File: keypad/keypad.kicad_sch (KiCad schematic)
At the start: 0 parts

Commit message: Scheme 1.0 complete
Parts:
- added C1, C2, C3, C4: 0.1u, symbol Device:C_Small
- added C5: 10u, symbol Device:C_Small
- added C? (x2): 22p, symbol Device:C_Small
- added C?: 1u, symbol Device:C_Small
- added F?: 500mA, symbol Device:Polyfuse_Small
- added J?: AVR-ISP-6, symbol Connector:AVR-ISP-6
- added R? (x2): 5.1k, symbol Device:R_Small
- added R? (x2): 22, symbol Device:R_Small
- added R? (x2): 10k, symbol Device:R_Small
- added SW?: SW_Push_Reset, symbol SW_SKQG:SW_SKQG
- added U?: PRTR5V0U2X, symbol random-keyboard-parts:PRTR5V0U2X
- added U?: ATMEGA32U4-AU, QFP80P1200X1200X120-44N, symbol ATMEGA32U4-AU:ATMEGA32U4-AU
- added USB?: HRO-TYPE-C-31-M-12, symbol Type-C:HRO-TYPE-C-31-M-12
- added Y?: XTAL, symbol Device:Crystal_GND24_Small
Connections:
- new net: R?.2, USB?.4 (CC1)
- new net: R?.2, USB?.10 (CC2)
- new net: R?.1, U?.3 (IO2), USB?.5 (DN2), USB?.7 (DN1)
- new net: R?.1, U?.2 (IO1), USB?.6 (DP1), USB?.8 (DP2)
- new net: R?.1, U?.33 (PE2)
- new net: C?.1, U?.6 (UCAP)
- new net +5V: C1.1, C2.1, C3.1, C4.1, C5.1, F?.2, J?.2 (VCC), R?.1, U?.14 (VCC), U?.2 (UVCC), U?.24 (AVCC), U?.34 (VCC), U?.44 (AVCC), U?.7 (VBUS)
- new net D+: R?.2, U?.4 (D+)
- new net D-: R?.2, U?.3 (D-)
- new net GND: C1.2, C2.2, C3.2, C4.2, C5.2, C?.2, C?.2, C?.2, J?.6 (GND), R?.1, R?.1, R?.2, SW?.2 (ve), U?.1 (GND), U?.15 (GND), U?.23 (GND), U?.35 (GND), U?.43 (GND), U?.5 (UGND), USB?.1 (GND), USB?.12 (GND), USB?.13 (SHIELD), Y?.2, Y?.4
- new net MISO: J?.1 (MISO), U?.11 (PB3)
- new net MOSI: J?.4 (MOSI), U?.10 (PB2)
- new net Reset: J?.5 (~{RST}), R?.2, SW?.1 (ve), U?.13 (~{RESET})
- new net SCK: J?.3 (SCK), U?.9 (PB1)
- new net VCC: F?.1, U?.4 (VCC), USB?.11 (VBUS), USB?.2 (VBUS)
- new net XTAL1: C?.1, U?.17 (XTAL1), Y?.1
- new net XTAL2: C?.1, U?.16 (XTAL2), Y?.3
- no-connect marks 0 -> 5

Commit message: Creat Matrix 1.0
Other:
- added sheet matrix (matrix.kicad_sch)
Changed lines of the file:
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@@
     (pin "2")
+  )
+  (sheet (at 260.35 158.75) (size 12.7 3.81) (fields_autoplaced)
+    (stroke (width 0.1524) (type solid) (color 0 0 0 0))
+    (fill (color 0 0 0 0.0000))
+    (property "Sheet name" "matrix" (id 0) (at 260.35 158.0384 0)
+      (effects (font (size 1.27 1.27)) (justify left bottom))
+    )
+    (property "Sheet file" "matrix.kicad_sch" (id 1) (at 260.35 163.1446 0)
+      (effects (font (size 1.27 1.27)) (justify left top))
+    )
   )
   (sheet_instances
     (path "/" (page "1"))
+    (path "/5536efe7-c8bb-4c6c-93af-3db80ade0fb5" (page "2"))
   )
   (symbol_instances
@@
       (reference "C?") (unit 1) (value "22p") (footprint "")
     )
+    (path "/5536efe7-c8bb-4c6c-93af-3db80ade0fb5/9a644794-52ea-4327-bd09-f8b15524fedf"
+      (reference "D1") (unit 1) (value "D") (footprint "")
+    )
+    (path "/5536efe7-c8bb-4c6c-93af-3db80ade0fb5/b4841a33-c386-479d-996e-ba2927116e58"
+      (reference "D2") (unit 1) (value "D") (footprint "")
+    )
+    (path "/5536efe7-c8bb-4c6c-93af-3db80ade0fb5/79e7db55-38f0-4a73-ab95-a7bab10db2bc"
+      (reference "D3") (unit 1) (value "D") (footprint "")
+    )
+    (path "/5536efe7-c8bb-4c6c-93af-3db80ade0fb5/f561a5ac-3059-4521-99af-42498ff48bbe"
+      (reference "D4") (unit 1) (value "D") (footprint "")
+    )
+    (path "/5536efe7-c8bb-4c6c-93af-3db80ade0fb5/c448c4ba-7a95-4e8b-868a-fbc34300787c"
+      (reference "D5") (unit 1) (value "D") (footprint "")
+    )
+    (path "/5536efe7-c8bb-4c6c-93af-3db80ade0fb5/e07c9ef6-5451-425c-9e0a-962144539f5d"
+      (reference "D6") (unit 1) (value "D") (footprint "")
+    )
+    (path "/5536efe7-c8bb-4c6c-93af-3db80ade0fb5/78d23edb-643f-406e-b146-b9943f76ab45"
+      (reference "D7") (unit 1) (value "D") (footprint "")
+    )
+    (path "/5536efe7-c8bb-4c6c-93af-3db80ade0fb5/89fcd485-e50f-416d-9f08-898bba03eec0"
+      (reference "D8") (unit 1) (value "D") (footprint "")
+    )
+    (path "/5536efe7-c8bb-4c6c-93af-3db80ade0fb5/7c6547ba-1358-4c6c-8003-39bdd1f7d938"
+      (reference "D9") (unit 1) (value "D") (footprint "")
+    )
+    (path "/5536efe7-c8bb-4c6c-93af-3db80ade0fb5/67ecc62a-8f0d-4b3a-b4c1-b1c6e1ca890f"
+      (reference "D10") (unit 1) (value "D") (footprint "")
+    )
+    (path "/5536efe7-c8bb-4c6c-93af-3db80ade0fb5/bc75af07-bd2c-4b47-b0fb-1f1929983761"
+      (reference "D11") (unit 1) (value "D") (footprint "")
+    )
+    (path "/5536efe7-c8bb-4c6c-93af-3db80ade0fb5/280455c7-3c8b-418f-a011-da03396841a7"
+      (reference "D12") (unit 1) (value "D") (footprint "")
+    )
+    (path "/5536efe7-c8bb-4c6c-93af-3db80ade0fb5/c2839c0b-9c65-4167-8039-ba7e2d9fec9d"
+      (reference "D13") (unit 1) (value "D") (footprint "")
+    )
+    (path "/5536efe7-c8bb-4c6c-93af-3db80ade0fb5/de303921-c38f-4c10-aba0-b46505fdefbf"
+      (reference "D14") (unit 1) (value "D") (footprint "")
+    )
+    (path "/5536efe7-c8bb-4c6c-93af-3db80ade0fb5/bdbe8408-effe-4323-8624-7153e57df912"
+      (reference "D15") (unit 1) (value "D") (footprint "")
+    )
+    (path "/5536efe7-c8bb-4c6c-93af-3db80ade0fb5/687984bd-da5f-4098-8907-2694332a2741"
+      (reference "D16") (unit 1) (value "D") (footprint "")
+    )
+    (path "/5536efe7-c8bb-4c6c-93af-3db80ade0fb5/72dba145-79d1-42aa-a952-0fcd5dbb5f51"
+      (reference "D17") (unit 1) (value "D") (footprint "")
+    )
+    (path "/5536efe7-c8bb-4c6c-93af-3db80ade0fb5/359023dd-c07d-4d1f-8a68-2798543f6791"
+      (reference "D18") (unit 1) (value "D") (footprint "")
+    )
+    (path "/5536efe7-c8bb-4c6c-93af-3db80ade0fb5/ec1a4f44-ed28-469d-bce4-39f6b11d96b0"
+      (reference "D19") (unit 1) (value "D") (footprint "")
+    )
     (path "/8191da82-1b24-43f7-89f2-5c294481326b"
       (reference "F?") (unit 1) (value "500mA") (footprint "")
@@
       (reference "R?") (unit 1) (value "22") (footprint "")
     )
+    (path "/5536efe7-c8bb-4c6c-93af-3db80ade0fb5/a8fbe275-e45a-4f46-aab6-af2a9be66cc7"
+      (reference "SW1") (unit 1) (value "num") (footprint "")
+    )
+    (path "/5536efe7-c8bb-4c6c-93af-3db80ade0fb5/90daedf7-5a7f-4c03-b61a-54b82546f0ae"
+      (reference "SW2") (unit 1) (value "div") (footprint "")
+    )
+    (path "/5536efe7-c8bb-4c6c-93af-3db80ade0fb5/6320b691-9818-4d75-b444-8163a922571d"
+      (reference "SW3") (unit 1) (value "mult") (footprint "")
+    )
+    (path "/5536efe7-c8bb-4c6c-93af-3db80ade0fb5/52d3a178-efab-47c5-a04f-7b9702ec7191"
+      (reference "SW4") (unit 1) (value "min") (footprint "")
+    )
+    (path "/5536efe7-c8bb-4c6c-93af-3db80ade0fb5/900f3076-96ff-42d7-a6f8-6e5918b538b7"
+      (reference "SW5") (unit 1) (value "#7") (footprint "")
+    )
+    (path "/5536efe7-c8bb-4c6c-93af-3db80ade0fb5/3423f380-322d-4e75-85ef-f42ce1034340"
+      (reference "SW6") (unit 1) (value "#8") (footprint "")
+    )
+    (path "/5536efe7-c8bb-4c6c-93af-3db80ade0fb5/b9ef477f-6510-4722-bbd5-47ed3b264249"
+      (reference "SW7") (unit 1) (value "#9") (footprint "")
+    )
+    (path "/5536efe7-c8bb-4c6c-93af-3db80ade0fb5/af993652-e2ec-4985-b2d6-324ab2415001"
+      (reference "SW8") (unit 1) (value "plu0") (footprint "")
+    )
+    (path "/5536efe7-c8bb-4c6c-93af-3db80ade0fb5/5a9c176c-6c6a-40aa-a0cf-ecfca809a92a"
+      (reference "SW9") (unit 1) (value "#4") (footprint "")
+    )
+    (path "/5536efe7-c8bb-4c6c-93af-3db80ade0fb5/49aa3199-5925-426d-9bbe-c5416226cedc"
+      (reference "SW10") (unit 1) (value "#5") (footprint "")
+    )
+    (path "/5536efe7-c8bb-4c6c-93af-3db80ade0fb5/edbfbc9f-fae0-4b09-8fd1-2fdb5910af52"
+      (reference "SW11") (unit 1) (value "#6") (footprint "")
+    )
+    (path "/5536efe7-c8bb-4c6c-93af-3db80ade0fb5/dd21500d-5cc3-406f-b6e4-1ac6ec593097"
+      (reference "SW12") (unit 1) (value "plu1") (footprint "")
+    )
+    (path "/5536efe7-c8bb-4c6c-93af-3db80ade0fb5/ba03b49d-f73d-4109-b19f-516cb2f4d6fa"
+      (reference "SW13") (unit 1) (value "#1") (footprint "")
+    )
+    (path "/5536efe7-c8bb-4c6c-93af-3db80ade0fb5/f13ec7a5-97d7-4169-806d-f29da36b319b"
+      (reference "SW14") (unit 1) (value "#2") (footprint "")
+    )
+    (path "/5536efe7-c8bb-4c6c-93af-3db80ade0fb5/e85cc504-ce98-4080-8b0a-822b1039c0be"
+      (reference "SW15") (unit 1) (value "#3") (footprint "")
+    )
+    (path "/5536efe7-c8bb-4c6c-93af-3db80ade0fb5/2dd3eeeb-1dda-4560-a555-7533fb4ee835"
+      (reference "SW16") (unit 1) (value "ent0") (footprint "")
+    )
+    (path "/5536efe7-c8bb-4c6c-93af-3db80ade0fb5/eb663575-2bb7-46c4-8857-4495de8fb975"
+      (reference "SW17") (unit 1) (value "#0") (footprint "")
+    )
+    (path "/5536efe7-c8bb-4c6c-93af-3db80ade0fb5/34938f56-f0c5-42e4-858d-1eefaa7132ef"
+      (reference "SW18") (unit 1) (value "kom") (footprint "")
+    )
+    (path "/5536efe7-c8bb-4c6c-93af-3db80ade0fb5/d07f8cae-5702-4915-8b31-407c3d188184"
+      (reference "SW19") (unit 1) (value "ent1") (footprint "")
+    )
     (path "/df8a378d-e0e9-4784-8be5-a23e7f34a8f8"

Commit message: Assign Footprints
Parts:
- C1, C2, C8: renamed from C?; footprint (none) -> Capacitor_SMD:C_0805_2012Metric_Pad1.18x1.45mm_HandSolder
- C3: renamed from C1; footprint (none) -> Capacitor_SMD:C_0805_2012Metric_Pad1.18x1.45mm_HandSolder
- C4: renamed from C2; footprint (none) -> Capacitor_SMD:C_0805_2012Metric_Pad1.18x1.45mm_HandSolder
- C5: renamed from C3; footprint (none) -> Capacitor_SMD:C_0805_2012Metric_Pad1.18x1.45mm_HandSolder
- C6: renamed from C4; footprint (none) -> Capacitor_SMD:C_0805_2012Metric_Pad1.18x1.45mm_HandSolder
- C7: renamed from C5; footprint (none) -> Capacitor_SMD:C_0805_2012Metric_Pad1.18x1.45mm_HandSolder
- F1: renamed from F?; footprint (none) -> Fuse:Fuse_1206_3216Metric_Pad1.42x1.75mm_HandSolder
- J1: renamed from J?; footprint (none) -> random-keyboard-parts:Reset_Pretty-Mask
- R1, R2, R3, R4, R5, R6: renamed from R?; footprint (none) -> Resistor_SMD:R_0805_2012Metric_Pad1.20x1.40mm_HandSolder
- SW20: renamed from SW?; footprint (none) -> Button_Switch_SMD:SW_SPST_SKQG_WithStem
- U1: renamed from U?; footprint (none) -> random-keyboard-parts:SOT143B
- U2: renamed from U?; footprint QFP80P1200X1200X120-44N -> ATMEGA32U4-AU:QFP80P1200X1200X120-44N
- USB1: renamed from USB?; footprint (none) -> Type-C:HRO-TYPE-C-31-M-12-HandSoldering
- Y1: renamed from Y?; footprint (none) -> Crystal:Crystal_SMD_3225-4Pin_3.2x2.5mm_HandSoldering
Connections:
- net col2: now reaches U2.29 (PB5)
- net col3: now reaches U2.30 (PB6)
- net col1: now reaches U2.31 (PC6)
- net col0: now reaches U2.32 (PC7)
- net row4: now reaches U2.37 (PF6)
- net row3: now reaches U2.38 (PF5)
- net row2: now reaches U2.39 (PF4)
- net row1: now reaches U2.40 (PF1)
- net row0: now reaches U2.41 (PF0)
- no-connect marks 5 -> 18

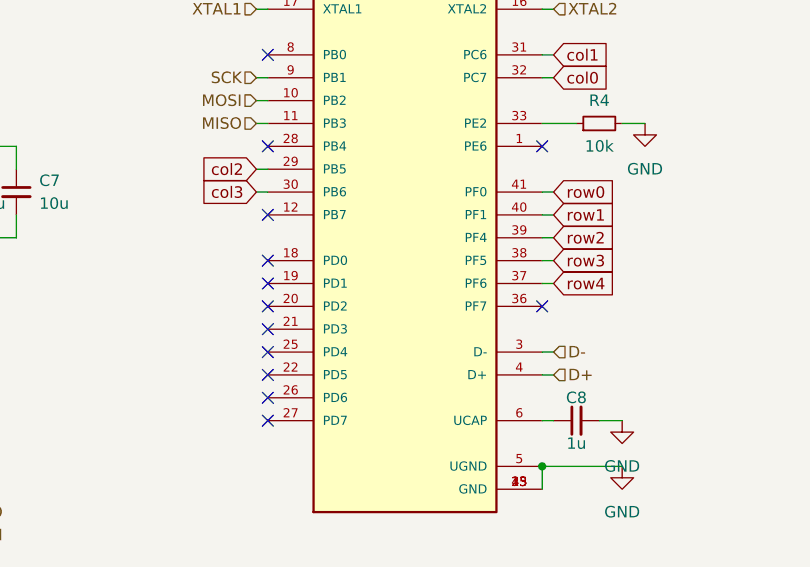
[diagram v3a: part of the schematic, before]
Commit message: Fixed Layering
Also as a note, there was a rogue 1uF capacitor which I now just placed under the usb, out of the way. It may be needed later.
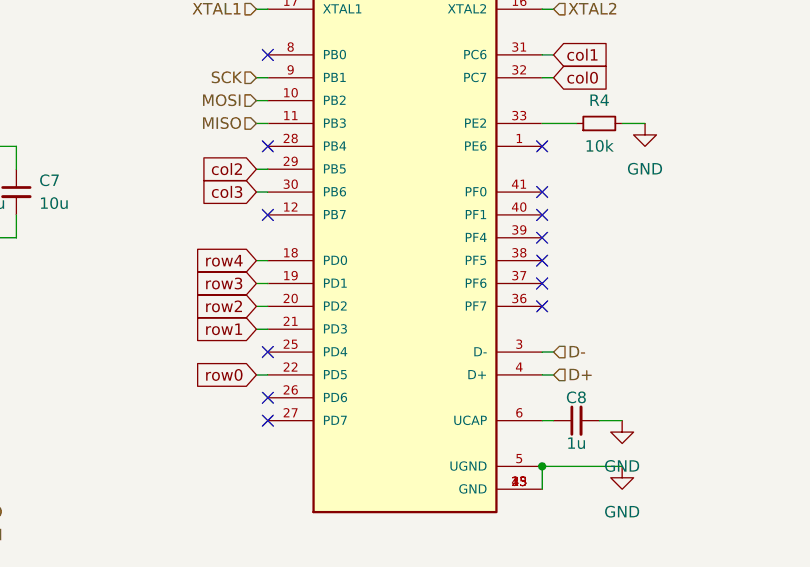
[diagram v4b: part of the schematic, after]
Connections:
- net row0: now also U2.22 (PD5); no longer U2.41 (PF0)
- net row1: now also U2.21 (PD3); no longer U2.40 (PF1)
- net row2: now also U2.20 (PD2); no longer U2.39 (PF4)
- net row3: now also U2.19 (PD1); no longer U2.38 (PF5)
- net row4: now also U2.18 (PD0); no longer U2.37 (PF6)
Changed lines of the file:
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@@
   (no_connect (at 63.5 68.58))
   (no_connect (at 129.54 109.22))
-  (no_connect (at 99.06 109.22))
+  (no_connect (at 129.54 101.6))
   (no_connect (at 207.01 68.58))
-  (no_connect (at 99.06 111.76))
   (no_connect (at 99.06 81.28))
+  (no_connect (at 129.54 99.06))
   (no_connect (at 99.06 91.44))
   (no_connect (at 99.06 68.58))
   (no_connect (at 50.8 63.5))
   (no_connect (at 99.06 119.38))
-  (no_connect (at 99.06 104.14))
-  (no_connect (at 99.06 116.84))
   (no_connect (at 129.54 91.44))
   (no_connect (at 207.01 83.82))
   (no_connect (at 99.06 121.92))
+  (no_connect (at 129.54 104.14))
   (no_connect (at 99.06 99.06))
+  (no_connect (at 129.54 96.52))
   (no_connect (at 99.06 114.3))
-  (no_connect (at 99.06 106.68))
+  (no_connect (at 129.54 106.68))
   (wire (pts (xy 71.12 93.98) (xy 71.12 91.44))
     (stroke (width 0) (type default) (color 0 0 0 0))
@@
     (stroke (width 0) (type default) (color 0 0 0 0))
   )
+  (wire (pts (xy 97.79 104.14) (xy 99.06 104.14))
+    (stroke (width 0) (type default) (color 0 0 0 0))
+  )
   (wire (pts (xy 63.5 63.5) (xy 64.77 63.5))
     (stroke (width 0) (type default) (color 0 0 0 0))
@@
     (stroke (width 0) (type default) (color 0 0 0 0))
   )
-  (wire (pts (xy 129.54 96.52) (xy 130.81 96.52))
-    (stroke (width 0) (type default) (color 0 0 0 0))
-  )
   (wire (pts (xy 207.01 86.36) (xy 214.63 86.36))
     (stroke (width 0) (type default) (color 0 0 0 0))
@@
     (stroke (width 0) (type default) (color 0 0 0 0))
   )
+  (wire (pts (xy 97.79 116.84) (xy 99.06 116.84))
+    (stroke (width 0) (type default) (color 0 0 0 0))
+  )
   (wire (pts (xy 208.28 63.5) (xy 208.28 91.44))
     (stroke (width 0) (type default) (color 0 0 0 0))
@@
     (stroke (width 0) (type default) (color 0 0 0 0))
   )
-  (wire (pts (xy 129.54 99.06) (xy 130.81 99.06))
-    (stroke (width 0) (type default) (color 0 0 0 0))
-  )
   (wire (pts (xy 85.09 45.72) (xy 85.09 46.99))
     (stroke (width 0) (type default) (color 0 0 0 0))
@@
     (stroke (width 0) (type default) (color 0 0 0 0))
   )
+  (wire (pts (xy 97.79 111.76) (xy 99.06 111.76))
+    (stroke (width 0) (type default) (color 0 0 0 0))
+  )
   (wire (pts (xy 71.12 101.6) (xy 63.5 101.6))
     (stroke (width 0) (type default) (color 0 0 0 0))
@@
     (stroke (width 0) (type default) (color 0 0 0 0))
   )
-  (wire (pts (xy 129.54 104.14) (xy 130.81 104.14))
+  (wire (pts (xy 97.79 109.22) (xy 99.06 109.22))
     (stroke (width 0) (type default) (color 0 0 0 0))
   )
@@
     (stroke (width 0) (type default) (color 0 0 0 0))
   )
+  (wire (pts (xy 97.79 106.68) (xy 99.06 106.68))
+    (stroke (width 0) (type default) (color 0 0 0 0))
+  )
   (wire (pts (xy 87.63 43.18) (xy 91.44 43.18))
     (stroke (width 0) (type default) (color 0 0 0 0))
@@
     (stroke (width 0) (type default) (color 0 0 0 0))
   )
-  (wire (pts (xy 129.54 101.6) (xy 130.81 101.6))
-    (stroke (width 0) (type default) (color 0 0 0 0))
-  )
   (wire (pts (xy 208.28 93.98) (xy 212.09 93.98))
     (stroke (width 0) (type default) (color 0 0 0 0))
   )
-  (wire (pts (xy 129.54 106.68) (xy 130.81 106.68))
-    (stroke (width 0) (type default) (color 0 0 0 0))
-  )
   (wire (pts (xy 213.36 76.2) (xy 213.36 81.28))
     (stroke (width 0) (type default) (color 0 0 0 0))
@@
     (stroke (width 0) (type default) (color 0 0 0 0))
   )
-  (global_label "row4" (shape input) (at 130.81 106.68 0) (fields_autoplaced)
-    (effects (font (size 1.27 1.27)) (justify left))
-    (property "Intersheet References" "${INTERSHEET_REFS}" (id 0) (at 137.6983 106.6006 0)
-      (effects (font (size 1.27 1.27)) (justify left) hide)
+  (global_label "row4" (shape input) (at 97.79 104.14 180) (fields_autoplaced)
+    (effects (font (size 1.27 1.27)) (justify right))
+    (property "Intersheet References" "${INTERSHEET_REFS}" (id 0) (at 90.9017 104.2194 0)
+      (effects (font (size 1.27 1.27)) (justify right) hide)
     )
   )
@@
     )
   )
-  (global_label "row1" (shape input) (at 130.81 99.06 0) (fields_autoplaced)
-    (effects (font (size 1.27 1.27)) (justify left))
-    (property "Intersheet References" "${INTERSHEET_REFS}" (id 0) (at 137.6983 98.9806 0)
-      (effects (font (size 1.27 1.27)) (justify left) hide)
-    )
-  )
-  (global_label "row0" (shape input) (at 130.81 96.52 0) (fields_autoplaced)
-    (effects (font (size 1.27 1.27)) (justify left))
-    (property "Intersheet References" "${INTERSHEET_REFS}" (id 0) (at 137.6983 96.4406 0)
-      (effects (font (size 1.27 1.27)) (justify left) hide)
-    )
-  )
-  (global_label "row2" (shape input) (at 130.81 101.6 0) (fields_autoplaced)
-    (effects (font (size 1.27 1.27)) (justify left))
-    (property "Intersheet References" "${INTERSHEET_REFS}" (id 0) (at 137.6983 101.5206 0)
-      (effects (font (size 1.27 1.27)) (justify left) hide)
+  (global_label "row1" (shape input) (at 97.79 111.76 180) (fields_autoplaced)
+    (effects (font (size 1.27 1.27)) (justify right))
+    (property "Intersheet References" "${INTERSHEET_REFS}" (id 0) (at 90.9017 111.8394 0)
+      (effects (font (size 1.27 1.27)) (justify right) hide)
+    )
+  )
+  (global_label "row0" (shape input) (at 97.79 116.84 180) (fields_autoplaced)
+    (effects (font (size 1.27 1.27)) (justify right))
+    (property "Intersheet References" "${INTERSHEET_REFS}" (id 0) (at 90.9017 116.9194 0)
+      (effects (font (size 1.27 1.27)) (justify right) hide)
+    )
+  )
+  (global_label "row2" (shape input) (at 97.79 109.22 180) (fields_autoplaced)
+    (effects (font (size 1.27 1.27)) (justify right))
+    (property "Intersheet References" "${INTERSHEET_REFS}" (id 0) (at 90.9017 109.2994 0)
+      (effects (font (size 1.27 1.27)) (justify right) hide)
     )
   )
@@
     )
   )
-  (global_label "row3" (shape input) (at 130.81 104.14 0) (fields_autoplaced)
-    (effects (font (size 1.27 1.27)) (justify left))
-    (property "Intersheet References" "${INTERSHEET_REFS}" (id 0) (at 137.6983 104.0606 0)
-      (effects (font (size 1.27 1.27)) (justify left) hide)
-    )
-  )
+  (global_label "row3" (shape input) (at 97.79 106.68 180) (fields_autoplaced)
+    (effects (font (size 1.27 1.27)) (justify right))
+    (property "Intersheet References" "${INTERSHEET_REFS}" (id 0) (at 90.9017 106.7594 0)
+      (effects (font (size 1.27 1.27)) (justify right) hide)
+    )
+  )

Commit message: Started Routing
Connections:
- net DN: now reaches R2.1, U1.3 (IO2), USB1.5 (DN2), USB1.7 (DN1)
- net DP: now reaches R3.1, U1.2 (IO1), USB1.6 (DP1), USB1.8 (DP2)
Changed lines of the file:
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@@
+    )
+  )
+  (global_label "DN" (shape input) (at 222.25 78.74 90) (fields_autoplaced)
+    (effects (font (size 1.27 1.27)) (justify left))
+    (property "Intersheet References" "${INTERSHEET_REFS}" (id 0) (at 222.1706 73.7264 90)
+      (effects (font (size 1.27 1.27)) (justify left) hide)
     )
   )
@@
       (effects (font (size 1.27 1.27)) (justify right) hide)
     )
+  )
+  (global_label "DP" (shape input) (at 222.25 81.28 270) (fields_autoplaced)
+    (effects (font (size 1.27 1.27)) (justify right))
+    (property "Intersheet References" "${INTERSHEET_REFS}" (id 0) (at 222.1706 86.2331 90)
+      (effects (font (size 1.27 1.27)) (justify right) hide)
+    )
